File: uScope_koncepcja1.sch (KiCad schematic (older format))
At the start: 20 parts

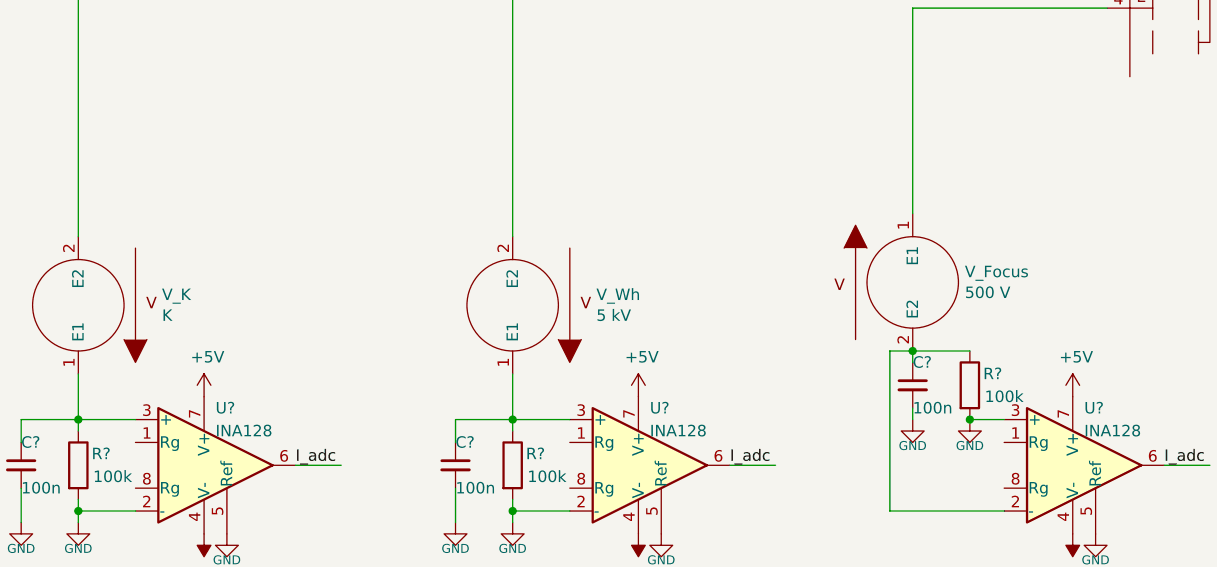
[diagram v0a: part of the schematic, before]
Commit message: - schematic as hierarchical - added cache lib
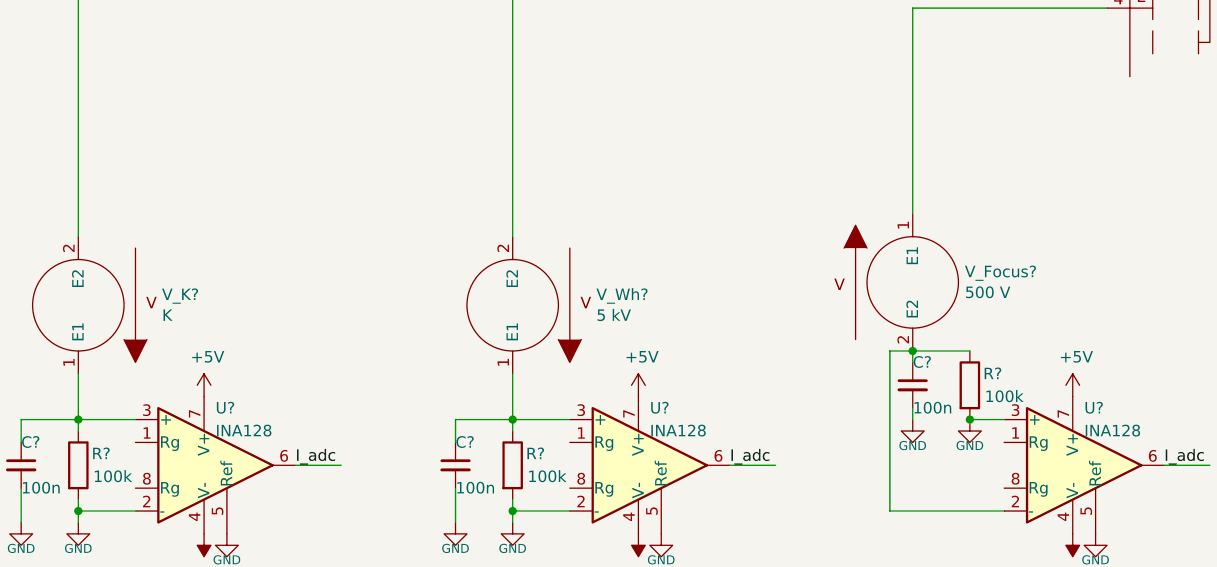
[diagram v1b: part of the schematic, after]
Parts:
- renumbered V_Focus to V_Focus?, V_K to V_K?, V_Wh to V_Wh?
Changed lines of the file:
@@
 $Descr A4 11693 8268
 encoding utf-8
-Sheet 1 1
+Sheet 1 5
 Title ""
 Date "2020-08-14"
@@
 $EndComp
 $Comp
-L pspice:VSOURCE V_K
+L pspice:VSOURCE V_K?
 U 1 1 5F36B478
 P 1150 4200
-F 0 "V_K" H 784 4154 50  0000 R CNN
+F 0 "V_K?" H 784 4154 50  0000 R CNN
 F 1 "K" H 784 4245 50  0000 R CNN
 F 2 "" H 1150 4200 50  0001 C CNN
@@
 $EndComp
 $Comp
-L pspice:VSOURCE V_Wh
+L pspice:VSOURCE V_Wh?
 U 1 1 5F36B607
 P 3050 4200
-F 0 "V_Wh" H 2684 4154 50  0000 R CNN
+F 0 "V_Wh?" H 2684 4154 50  0000 R CNN
 F 1 "5 kV" H 2684 4245 50  0000 R CNN
 F 2 "" H 3050 4200 50  0001 C CNN
@@
 $EndComp
 $Comp
-L pspice:VSOURCE V_Focus
+L pspice:VSOURCE V_Focus?
 U 1 1 5F36B645
 P 4800 4100
-F 0 "V_Focus" H 5028 4146 50  0000 L CNN
+F 0 "V_Focus?" H 5028 4146 50  0000 L CNN
 F 1 "500 V" H 5028 4055 50  0000 L CNN
 F 2 "" H 4800 4100 50  0001 C CNN

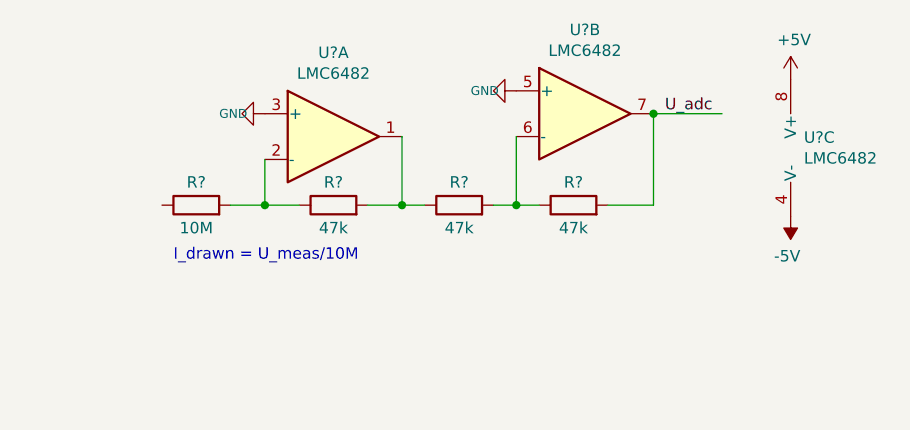
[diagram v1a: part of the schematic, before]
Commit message: - moved voltmeters to separate sheet - hierarchical sheets
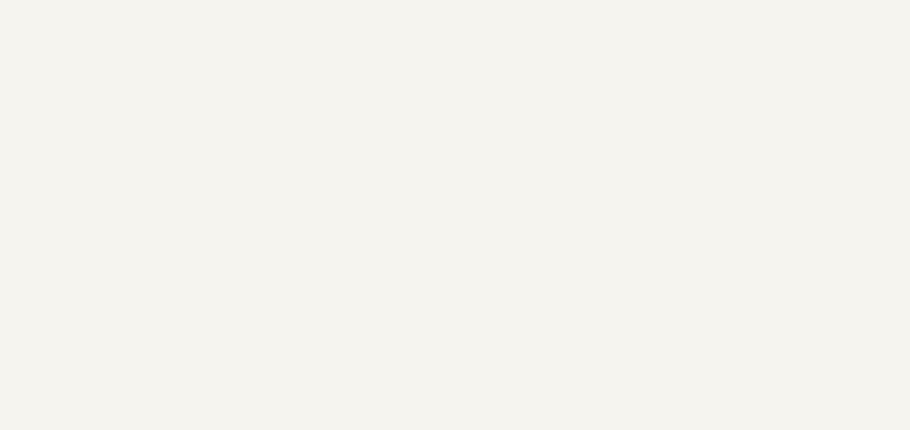
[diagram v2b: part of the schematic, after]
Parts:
- removed R? (x3): 47k, symbol Device:R
- removed R?: 10M, symbol Device:R
- removed U? (x3): LMC6482, symbol Amplifier_Operational:LMC6482
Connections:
- net labels removed: U_adc
- wire segments 46 -> 34
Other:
- note removed: "I_drawn = U_meas/10M"
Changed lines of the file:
@@
 $Descr A4 11693 8268
 encoding utf-8
-Sheet 1 5
+Sheet 3 7
 Title ""
 Date "2020-08-14"
@@
 Wire Wire Line
 	1150 2150 5950 2150
-$Comp
-L Amplifier_Operational:LMC6482 U?
-U 1 1 5F36BD59
-P 7750 2650
-F 0 "U?" H 7750 3017 50  0000 C CNN
-F 1 "LMC6482" H 7750 2926 50  0000 C CNN
-F 2 "" H 7750 2650 50  0001 C CNN
-F 3 "http://www.ti.com/lit/ds/symlink/lmc6482.pdf" H 7750 2650 50  0001 C CNN
-	1    7750 2650
-	1    0    0    -1
-$EndComp
-$Comp
-L Amplifier_Operational:LMC6482 U?
-U 2 1 5F36BDC6
-P 8850 2550
-F 0 "U?" H 8850 2917 50  0000 C CNN
-F 1 "LMC6482" H 8850 2826 50  0000 C CNN
-F 2 "" H 8850 2550 50  0001 C CNN
-F 3 "http://www.ti.com/lit/ds/symlink/lmc6482.pdf" H 8850 2550 50  0001 C CNN
-	2    8850 2550
-	1    0    0    -1
-$EndComp
-$Comp
-L Amplifier_Operational:LMC6482 U?
-U 3 1 5F36BE38
-P 9850 2700
-F 0 "U?" H 9808 2746 50  0000 L CNN
-F 1 "LMC6482" H 9808 2655 50  0000 L CNN
-F 2 "" H 9850 2700 50  0001 C CNN
-F 3 "http://www.ti.com/lit/ds/symlink/lmc6482.pdf" H 9850 2700 50  0001 C CNN
-	3    9850 2700
-	1    0    0    -1
-$EndComp
-$Comp
-L Device:R R?
-U 1 1 5F36BEB0
-P 7750 2950
-F 0 "R?" V 7850 2950 50  0000 C CNN
-F 1 "47k" V 7650 2950 50  0000 C CNN
-F 2 "" V 7680 2950 50  0001 C CNN
-F 3 "~" H 7750 2950 50  0001 C CNN
-	1    7750 2950
-	0    -1   -1   0
-$EndComp
-$Comp
-L power:GND #PWR?
-U 1 1 5F36C004
-P 7450 2550
-F 0 "#PWR?" H 7450 2390 50  0001 C CNN
-F 1 "GND" V 7450 2473 39  0000 R CNN
-F 2 "" H 7450 2550 50  0001 C CNN
-F 3 "" H 7450 2550 50  0001 C CNN
-	1    7450 2550
-	0    1    1    0
-$EndComp
-$Comp
-L Device:R R?
-U 1 1 5F36C2B1
-P 7150 2950
-F 0 "R?" V 7250 2950 50  0000 C CNN
-F 1 "10M" V 7050 2950 50  0000 C CNN
-F 2 "" V 7080 2950 50  0001 C CNN
-F 3 "~" H 7150 2950 50  0001 C CNN
-	1    7150 2950
-	0    -1   -1   0
-$EndComp
-Wire Wire Line
-	7450 2750 7450 2950
-Wire Wire Line
-	7450 2950 7300 2950
-Wire Wire Line
-	7450 2950 7600 2950
-Connection ~ 7450 2950
-$Comp
-L Device:R R?
-U 1 1 5F36C4CE
-P 8300 2950
-F 0 "R?" V 8400 2950 50  0000 C CNN
-F 1 "47k" V 8200 2950 50  0000 C CNN
-F 2 "" V 8230 2950 50  0001 C CNN
-F 3 "~" H 8300 2950 50  0001 C CNN
-	1    8300 2950
-	0    -1   -1   0
-$EndComp
-$Comp
-L Device:R R?
-U 1 1 5F36C516
-P 8800 2950
-F 0 "R?" V 8900 2950 50  0000 C CNN
-F 1 "47k" V 8700 2950 50  0000 C CNN
-F 2 "" V 8730 2950 50  0001 C CNN
-F 3 "~" H 8800 2950 50  0001 C CNN
-	1    8800 2950
-	0    -1   -1   0
-$EndComp
-$Comp
-L power:GND #PWR?
-U 1 1 5F36C57F
-P 8550 2450
-F 0 "#PWR?" H 8550 2290 50  0001 C CNN
-F 1 "GND" V 8550 2373 39  0000 R CNN
-F 2 "" H 8550 2450 50  0001 C CNN
-F 3 "" H 8550 2450 50  0001 C CNN
-	1    8550 2450
-	0    1    1    0
-$EndComp
-Wire Wire Line
-	8150 2950 8050 2950
-Connection ~ 8050 2950
-Wire Wire Line
-	8450 2950 8550 2950
-Wire Wire Line
-	8550 2650 8550 2950
-Connection ~ 8550 2950
-Wire Wire Line
-	8550 2950 8650 2950
-Wire Wire Line
-	9150 2550 9150 2950
-Wire Wire Line
-	9150 2950 8950 2950
-$Comp
-L power:+5V #PWR?
-U 1 1 5F36C931
-P 9750 2400
-F 0 "#PWR?" H 9750 2250 50  0001 C CNN
-F 1 "+5V" H 9765 2573 50  0000 C CNN
-F 2 "" H 9750 2400 50  0001 C CNN
-F 3 "" H 9750 2400 50  0001 C CNN
-	1    9750 2400
-	1    0    0    -1
-$EndComp
-$Comp
-L power:-5V #PWR?
-U 1 1 5F36C989
-P 9750 3000
-F 0 "#PWR?" H 9750 3100 50  0001 C CNN
-F 1 "-5V" H 9765 3173 50  0000 C CNN
-F 2 "" H 9750 3000 50  0001 C CNN
-F 3 "" H 9750 3000 50  0001 C CNN
-	1    9750 3000
-	-1   0    0    1
-$EndComp
-Text Notes 7050 3200 0    50   ~ 0
-I_drawn = U_meas/10M
-Wire Wire Line
-	8050 2650 8050 2950
-Wire Wire Line
-	7900 2950 8050 2950
 $Comp
 L Device:R R?
@@
 I_adc
 Wire Wire Line
-	9150 2550 9450 2550
-Connection ~ 9150 2550
-Text Label 9200 2550 0    50   ~ 0
-U_adc
-Wire Wire Line
 	5200 4700 5050 4700
